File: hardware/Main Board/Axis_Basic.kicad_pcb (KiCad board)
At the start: 4 copper layers, 42 x 42 mm, 63 parts, among them J1 USB4105-GF-A, J2 JST_PH, J3 JST_PH, J4 S2B-PH-K-S, J5 1175-1628-ND, J6 1-84952-4, SW1 RKB2SJK, SW2 RKB2SJK, U1 TLV493D, U2 UA78M33CDCYR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

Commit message: missed connections
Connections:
- U3 pad 32: unconnected-(U3-PA15-Pad32) -> User_Input
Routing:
- net User_Input: track 7.09 -> 12.5 mm
- net +3.3V: track 47.9 -> 49.8 mm
- net GND: track 74.8 -> 74.4 mm, vias 102 -> 104

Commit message: Move pins for addressable LED
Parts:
- moved C14 0.36 mm to (148.0, 93.3)
- moved C16 0.36 mm to (150.0, 94.5)
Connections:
- J6 pad 11: PB05 -> PB07
- U3 pad 10: NEOPIX -> PB07
- U3 pad 6: PB05 -> NEOPIX
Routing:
- net PB07: track 0.00 -> 21.7 mm, vias 0 -> 2
- net PB05: track 11.7 -> 0.00 mm
- net NEOPIX: track 18.7 -> 19.5 mm
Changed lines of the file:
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@@
 	(net 74 "unconnected-(U3-PA19-Pad38)")
 	(net 75 "unconnected-(U3-PA20-Pad41)")
-	(net 76 "PB05")
+	(net 76 "PB07")
 	(net 77 "unconnected-(U3-PB22-Pad49)")
 	(net 78 "unconnected-(U3-PB23-Pad50)")
@@
 			(size 0.61 2)
 			(layers "F.Cu" "F.Paste" "F.Mask")
-			(net 76 "PB05")
+			(net 76 "PB07")
 			(pinfunction "Pin_11")
 			(pintype "passive")
@@
 			(layers "F.Cu" "F.Paste" "F.Mask")
 			(roundrect_rratio 0.25)
-			(net 76 "PB05")
+			(net 19 "NEOPIX")
 			(pinfunction "PB05")
 			(pintype "bidirectional")
@@
 			(layers "F.Cu" "F.Paste" "F.Mask")
 			(roundrect_rratio 0.25)
-			(net 19 "NEOPIX")
+			(net 76 "PB07")
 			(pinfunction "PB07")
 			(pintype "bidirectional")
@@
 	(footprint "Capacitor_SMD:C_0805_2012Metric"
 		(layer "F.Cu")
-		(at 148.3 93.5 135)
+		(at 148 93.3 135)
 		(descr "Capacitor SMD 0805 (2012 Metric), square (rectangular) end terminal, IPC_7351 nominal, (Body size source: IPC-SM-782 page 76, https://www.pcb-3d.com/wordpress/wp-content/uploads/ipc-sm-782a_amendment_1_and_2.pdf, https://docs.google.com/spreadsheets/d/1BsfQQcO9C6DZCsRaXUlFlo91Tg2WpOkGARC1WS5S8t0/edit?usp=sharing), generated with kicad-footprint-generator")
 		(tags "capacitor")
@@
 	(footprint "Capacitor_SMD:C_0402_1005Metric"
 		(layer "F.Cu")
-		(at 150.3 94.7 45)
+		(at 150 94.5 45)
 		(descr "Capacitor SMD 0402 (1005 Metric), square (rectangular) end terminal, IPC_7351 nominal, (Body size source: IPC-SM-782 page 76, https://www.pcb-3d.com/wordpress/wp-content/uploads/ipc-sm-782a_amendment_1_and_2.pdf), generated with kicad-footprint-generator")
 		(tags "capacitor")
@@
 	)
 	(segment
-		(start 146.2 95.1)
-		(end 147.031371 95.1)
-		(width 0.2)
-		(layer "F.Cu")
-		(net 19)
-	)
-	(segment
-		(start 135.3 89.2)
-		(end 140.3 89.2)
-		(width 0.2)
-		(layer "F.Cu")
-		(net 19)
-	)
-	(segment
-		(start 135.25 89.25)
-		(end 135.3 89.2)
-		(width 0.2)
-		(layer "F.Cu")
-		(net 19)
-	)
-	(segment
-		(start 147.031371 95.1)
-		(end 147.631371 95.7)
-		(width 0.2)
+		(start 152.279891 95.112124)
+		(end 152.279891 95.079891)
+		(width 0.25)
 		(layer "F.Cu")
 		(net 19)
 	)
 	(segment
-		(start 150.03934 95.7)
-		(end 150.865678 96.526338)
-		(width 0.2)
+		(start 152.279891 95.079891)
+		(end 146.4 89.2)
+		(width 0.25)
 		(layer "F.Cu")
 		(net 19)
 	)
 	(segment
-		(start 147.631371 95.7)
-		(end 150.03934 95.7)
-		(width 0.2)
+		(start 146.4 89.2)
+		(end 146.35 89.25)
+		(width 0.25)
 		(layer "F.Cu")
 		(net 19)
 	)
 	(segment
-		(start 140.3 89.2)
-		(end 146.2 95.1)
-		(width 0.2)
+		(start 146.35 89.25)
+		(end 135.25 89.25)
+		(width 0.25)
 		(layer "F.Cu")
 		(net 19)
@@
 	)
 	(segment
-		(start 152.279891 95.112124)
-		(end 146.6 89.432233)
+		(start 146.6 83.2)
+		(end 146.6 85.75)
 		(width 0.2)
 		(layer "F.Cu")
@@
 	)
 	(segment
-		(start 146.6 89.432233)
-		(end 146.6 85.75)
+		(start 147.7 95.7)
+		(end 147 95)
+		(width 0.2)
+		(layer "F.Cu")
+		(net 76)
+	)
+	(segment
+		(start 150.865678 96.526338)
+		(end 150.03934 95.7)
+		(width 0.2)
+		(layer "F.Cu")
+		(net 76)
+	)
+	(segment
+		(start 143.6 91.919239)
+		(end 143.6 91.7)
+		(width 0.2)
+		(layer "F.Cu")
+		(net 76)
+	)
+	(segment
+		(start 146.680761 95)
+		(end 143.6 91.919239)
+		(width 0.2)
+		(layer "F.Cu")
+		(net 76)
+	)
+	(segment
+		(start 147 95)
+		(end 146.680761 95)
+		(width 0.2)
+		(layer "F.Cu")
+		(net 76)
+	)
+	(segment
+		(start 150.03934 95.7)
+		(end 147.7 95.7)
 		(width 0.2)
 		(layer "F.Cu")
 		(net 76)
 	)
+	(via
+		(at 143.6 91.7)
+		(size 0.8)
+		(drill 0.4)
+		(layers "F.Cu" "B.Cu")
+		(net 76)
+	)
+	(via
+		(at 146.6 83.2)
+		(size 0.8)
+		(drill 0.4)
+		(layers "F.Cu" "B.Cu")
+		(net 76)
+	)
+	(segment
+		(start 143.6 91.7)
+		(end 143.6 86.2)
+		(width 0.2)
+		(layer "B.Cu")
+		(net 76)
+	)
+	(segment
+		(start 143.6 86.2)
+		(end 146.6 83.2)
+		(width 0.2)
+		(layer "B.Cu")
+		(net 76)
+	)

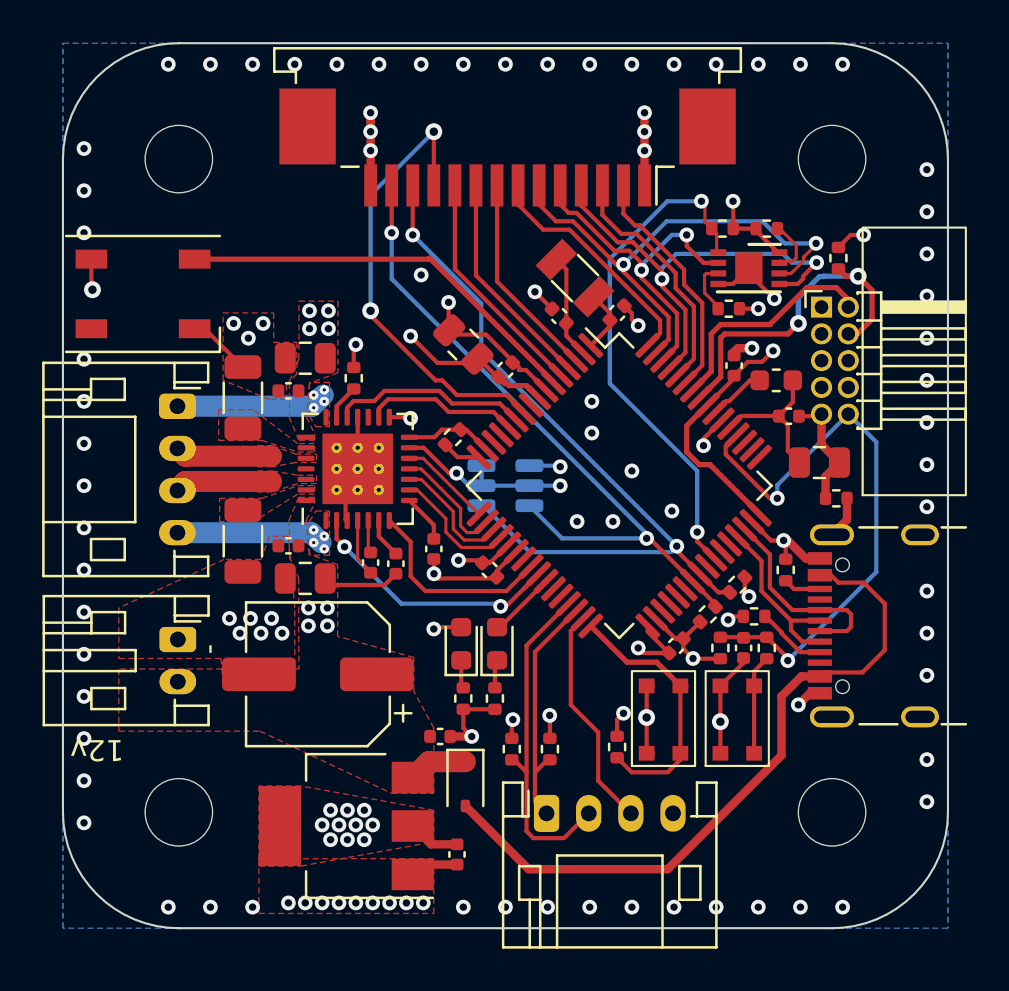
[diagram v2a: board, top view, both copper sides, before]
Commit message: Update SERCOM pins
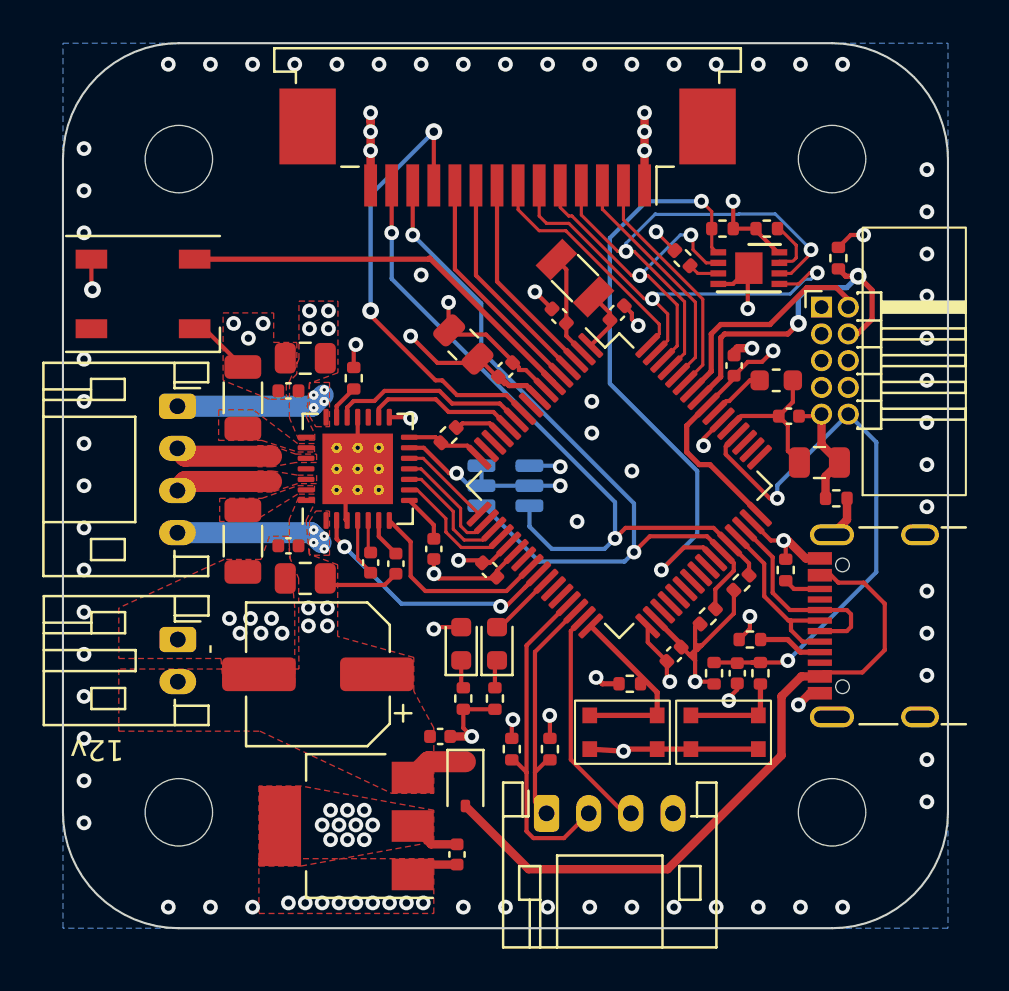
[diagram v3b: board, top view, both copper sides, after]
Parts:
- moved R11 3.26 mm to (158.4, 89.2), turned to -45 degrees
- moved R9 3.06 mm to (155.9, 109.4), turned to 0 degrees
- moved R19 2.19 mm to (161.2, 104.6)
- moved R20 2.05 mm to (159.6, 106.2), turned to 45 degrees
- moved SW2 1.99 mm to (155.6, 111.7), turned to 180 degrees
- moved C3 1.24 mm to (161.0, 108.9)
- moved R5 1.24 mm to (162.1, 108.9)
- moved R6 1.24 mm to (159.9, 108.9)
- moved R2 1.12 mm to (161.6, 107.3)
- moved SW1 0.85 mm to (160.4, 111.7), turned to 180 degrees
- moved C20 0.41 mm to (158.0, 108.0)
- moved R7 0.22 mm to (147.3, 97.6), turned to -135 degrees
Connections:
- C17 pad 2: Net-(U3-PA01) -> PA02
- J6 pad 4: MOSI -> SCK
- J6 pad 6: SCK -> MOSI
- U3 pad 13: unconnected-(U3-PA04-Pad13) -> UART_TX
- U3 pad 15: UART_RX -> unconnected-(U3-PA06/S0.2-Pad15)
- U3 pad 16: UART_TX -> UART_RX
- U3 pad 2: Net-(U3-PA01) -> PA02
- U3 pad 39: SDA1 -> unconnected-(U3-PB16/S5.0-Pad39)
- U3 pad 40: SCL1 -> unconnected-(U3-PB17/S5.1-Pad40)
- U3 pad 43: unconnected-(U3-PA22-Pad43) -> SCL1
- U3 pad 44: unconnected-(U3-PA23-Pad44) -> SDA1
- U3 pad 61: MOSI -> SCK
- U3 pad 63: SCK -> MOSI
- Y1 pad 2: Net-(U3-PA01) -> PA02
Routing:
- net +3.3V: track 49.8 -> 55.0 mm, vias 28 -> 27
- net PA02: track 9.85 -> 14.8 mm
- net Net-(U3-PA01): track 4.96 -> 0.00 mm
- net EEPROM_CS: track 24.5 -> 29.2 mm
- net User_Input: track 12.5 -> 8.75 mm
- net SCL1: track 36.1 -> 38.3 mm
- net SDA1: track 32.6 -> 34.7 mm
- net GND: track 74.4 -> 75.7 mm, vias 104 -> 102
- net Net-(U5-~{WP}): track 2.55 -> 1.49 mm
- net UART_RX: track 4.21 -> 3.70 mm
- net UART_TX: track 1.85 -> 2.35 mm
